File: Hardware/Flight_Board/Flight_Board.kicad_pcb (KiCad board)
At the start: 2 copper layers, 50.8 x 101.6 mm, 128 parts, among them J1 Conn_01x04, J2 Conn_01x08, J3 Conn_01x04, J4 Conn_01x06, J5 MEM2067-02-180-00-A_REVB, SW1 SW_Push, U1 FT5HN, U2 STM32F411RCTx, U3 ADXL375, U4 BMP390, U5 CAM-M8Q-0, U6 BMI323, U7 AP62200WU, U8 TPS274160A, U9 LR62E

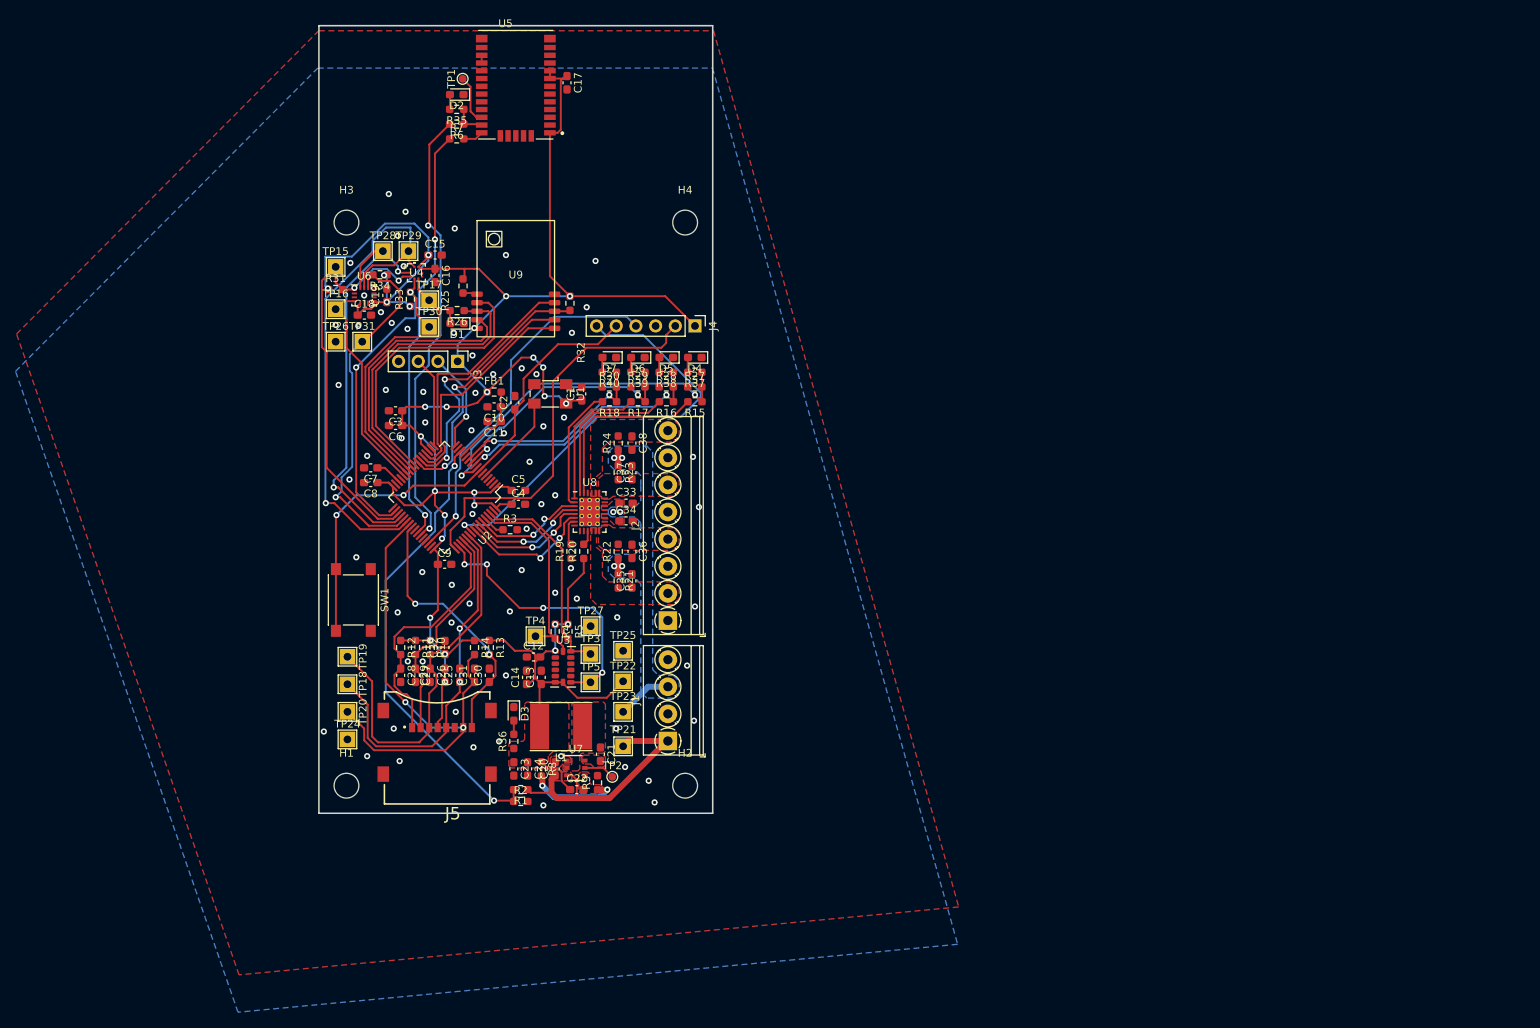
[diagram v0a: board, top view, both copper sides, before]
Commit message: begin 4 layer board
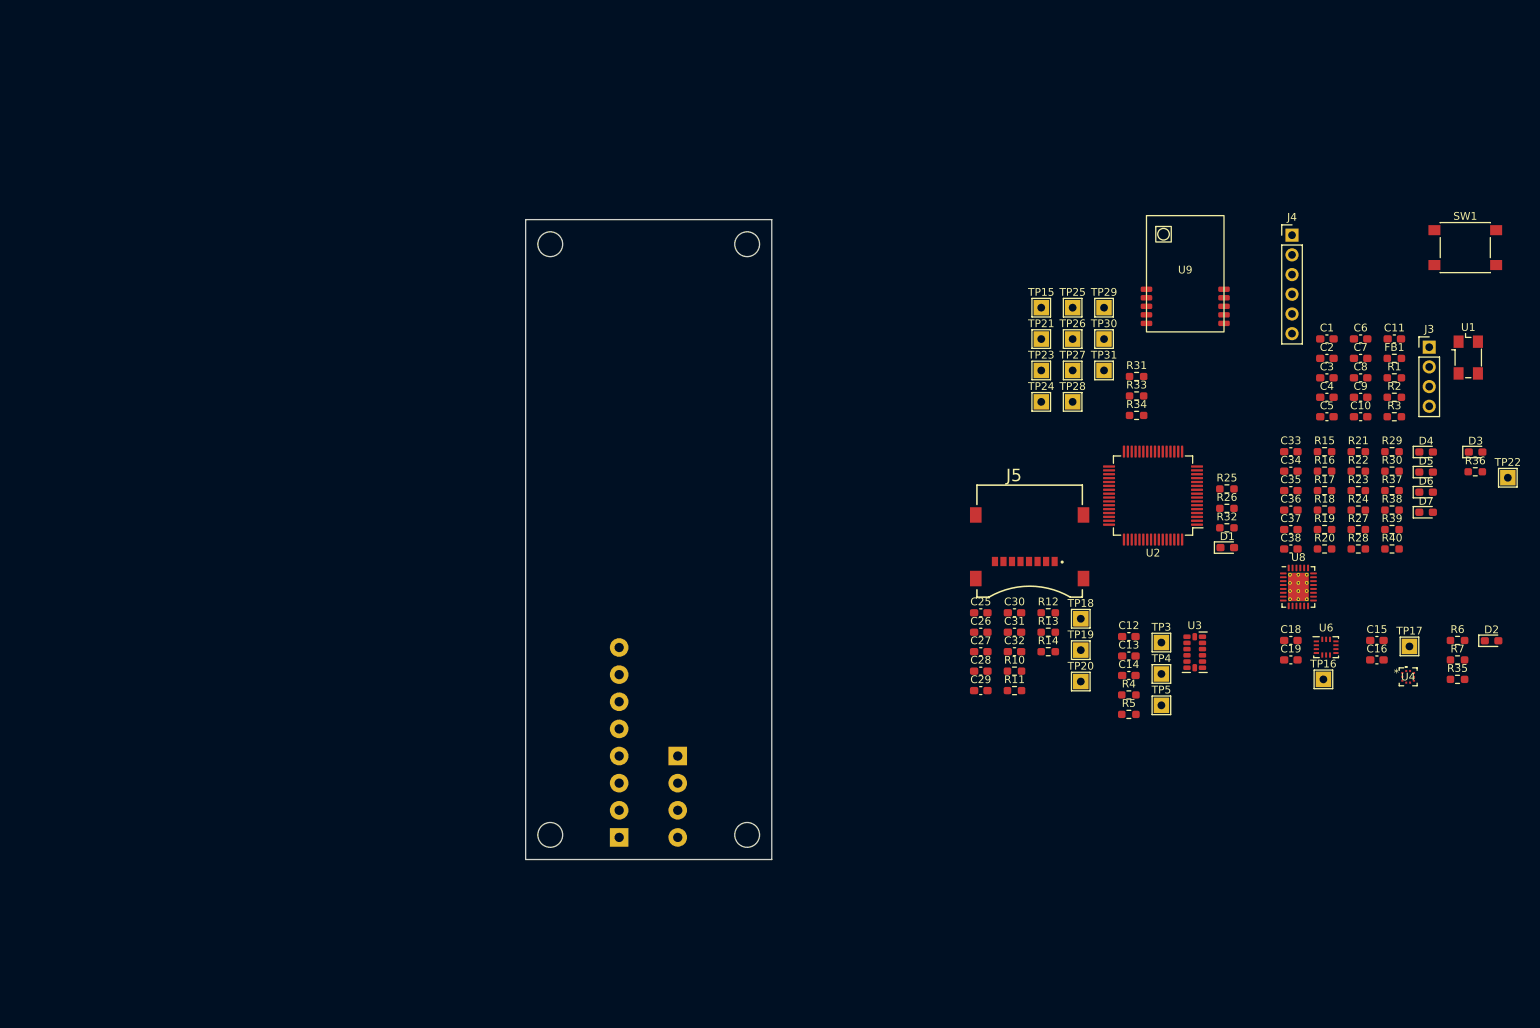
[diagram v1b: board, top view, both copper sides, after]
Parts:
- removed C17: 4.7u, Capacitor_SMD:C_0603_1608Metric_Pad1.08x0.95mm_HandSolder
- removed C20: 10u, Capacitor_SMD:C_0603_1608Metric_Pad1.08x0.95mm_HandSolder
- removed C21: 330n, Capacitor_SMD:C_0603_1608Metric_Pad1.08x0.95mm_HandSolder
- removed C22: 47p, Capacitor_SMD:C_0603_1608Metric_Pad1.08x0.95mm_HandSolder
- removed C23, C24: 22u, Capacitor_SMD:C_0603_1608Metric_Pad1.08x0.95mm_HandSolder
- removed L1: 4.7u, Inductor_SMD:L_Taiyo-Yuden_NR-60xx_HandSoldering
- removed R8: 31.6k, Resistor_SMD:R_0603_1608Metric_Pad0.98x0.95mm_HandSolder
- removed R9: 10k, Resistor_SMD:R_0603_1608Metric_Pad0.98x0.95mm_HandSolder
- removed TP1: SAFEBOOT, TestPoint:TestPoint_Pad_D1.0mm
- removed TP2: EN, TestPoint:TestPoint_Pad_D1.0mm
- removed U5: CAM-M8Q-0, Project:LCC100P960X1400X210-31N
- removed U7: AP62200WU, Package_SO:TSOP-6_1.65x3.05mm_P0.95mm
- H1, H2, H3, H4: footprint MountingHole:MountingHole_3.2mm_M3 -> MountingHole:MountingHole_3.2mm_M3_ISO14580
- J1, J2: moved to B.Cu
- moved D2 151.0 mm to (261.1, 117.8), turned to 0 degrees
- moved SW1 150.5 mm to (257.7, 67.1), turned to 0 degrees
- moved R35 148.6 mm to (256.7, 122.8), turned to 0 degrees
- moved R7 145.6 mm to (256.7, 120.3)
- moved R6 145.3 mm to (256.7, 117.8), turned to 0 degrees
- moved U4 138.2 mm to (250.4, 122.5)
- moved TP16 136.1 mm to (239.4, 122.8)
- moved TP17 134.1 mm to (250.5, 118.6)
- moved U6 132.1 mm to (239.8, 118.7)
- moved C15 131.3 mm to (246.3, 117.8)
- moved C16 131.2 mm to (246.3, 120.3), turned to 0 degrees
- moved R36 128.8 mm to (259.0, 96.0), turned to 0 degrees
- moved D3 128.6 mm to (259.1, 93.5), turned to 0 degrees
- moved C7 128.5 mm to (244.2, 81.4), turned to 0 degrees
- moved C8 128.4 mm to (244.2, 83.9), turned to 0 degrees
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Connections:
- R7 pad 2: Net-(U5-RXD/SPI_MOSI) -> unconnected-(R7-Pad2)
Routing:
- net +3.3V: track 308.4 -> 0.00 mm, vias 28 -> 0
- net /Barometer/SCK: track 68.4 -> 0.00 mm, vias 1 -> 0
- net /Microcontroller/NRST: track 64.8 -> 0.00 mm, vias 2 -> 0
- net /MicroSD/SDIO_D0: track 64.4 -> 0.00 mm, vias 2 -> 0
- net /GPS/TXD: track 60.2 -> 0.00 mm, vias 2 -> 0
- net /Microcontroller/VBAT_ADC: track 59.0 -> 0.00 mm, vias 2 -> 0
- net /Microcontroller/SWO: track 56.3 -> 0.00 mm, vias 1 -> 0
- net /Barometer/MOSI: track 55.6 -> 0.00 mm, vias 2 -> 0
- net /GPS/RXD: track 54.2 -> 0.00 mm, vias 2 -> 0
- net /Barometer/MISO: track 53.1 -> 0.00 mm, vias 2 -> 0
- net /Microcontroller/SWCLK: track 51.7 -> 0.00 mm
- net /MicroSD/SDIO_CMD: track 50.2 -> 0.00 mm
- net /IMU/~{CS}: track 47.4 -> 0.00 mm, vias 1 -> 0
- net /Microcontroller/SWDIO: track 47.1 -> 0.00 mm, vias 1 -> 0
- net /MicroSD/SDIO_CLK: track 46.7 -> 0.00 mm, vias 2 -> 0
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- added copper zone on In2.Cu, net +3.3V
- added copper zone on In1.Cu, net GND
- removed copper zone on F.Cu, net +3.3V
- removed copper zone on F.Cu, net /PYRO1
- removed copper zone on F.Cu, net /PYRO2
- removed copper zone on F.Cu, net /PYRO3
- removed copper zone on F.Cu, net /PYRO4
- removed copper zone on F.Cu, net /VBAT
- removed copper zone on B.Cu, net /VPYRO
- removed copper zone on F.Cu, net /VPYRO
- removed copper zone on B.Cu, net GND
- removed copper zone on F.Cu, net GND
- removed copper zone on F.Cu, net Net-(U7-BST)
- removed copper zone on F.Cu, net Net-(U7-FB)
- removed copper zone on F.Cu, net Net-(U7-SW)
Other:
- board size 50.8 x 101.6 mm -> 31.8 x 82.6 mm
- copper layers 2 -> 4

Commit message: initial route of 4-layer board
ouch
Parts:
- removed C2: 100n, Capacitor_SMD:C_0603_1608Metric_Pad1.08x0.95mm_HandSolder
- removed C37, C38: 22n, Capacitor_SMD:C_0603_1608Metric_Pad1.08x0.95mm_HandSolder
- removed D4: P1, LED_SMD:LED_0603_1608Metric_Pad1.05x0.95mm_HandSolder
- removed D5: P2, LED_SMD:LED_0603_1608Metric_Pad1.05x0.95mm_HandSolder
- removed D6: P3, LED_SMD:LED_0603_1608Metric_Pad1.05x0.95mm_HandSolder
- removed D7: P4, LED_SMD:LED_0603_1608Metric_Pad1.05x0.95mm_HandSolder
- removed R31, R32, R33, R34, R35, R36, R37, R38, R39, R40: 22k, Resistor_SMD:R_0603_1608Metric_Pad0.98x0.95mm_HandSolder
- removed SW1: SW_Push, Button_Switch_SMD:SW_SPST_PTS645
- removed TP15: MISO, TestPoint:TestPoint_THTPad_2.0x2.0mm_Drill1.0mm
- removed TP16: IMU_INT, TestPoint:TestPoint_THTPad_2.0x2.0mm_Drill1.0mm
- removed TP17: BARO_INT, TestPoint:TestPoint_THTPad_2.0x2.0mm_Drill1.0mm
- removed TP18: SD_CLK, TestPoint:TestPoint_THTPad_2.0x2.0mm_Drill1.0mm
- removed TP19: SD_CMD, TestPoint:TestPoint_THTPad_2.0x2.0mm_Drill1.0mm
- removed TP20: SD_D0, TestPoint:TestPoint_THTPad_2.0x2.0mm_Drill1.0mm
- removed TP21: VBAT, TestPoint:TestPoint_THTPad_2.0x2.0mm_Drill1.0mm
- removed TP22: 3V3, TestPoint:TestPoint_THTPad_2.0x2.0mm_Drill1.0mm
- removed TP23: VPYRO, TestPoint:TestPoint_THTPad_2.0x2.0mm_Drill1.0mm
- removed TP24, TP25, TP26, TP27: GND, TestPoint:TestPoint_THTPad_2.0x2.0mm_Drill1.0mm
- removed TP28: MOSI, TestPoint:TestPoint_THTPad_2.0x2.0mm_Drill1.0mm
- removed TP29: SCK, TestPoint:TestPoint_THTPad_2.0x2.0mm_Drill1.0mm
- removed TP3: SDA, TestPoint:TestPoint_THTPad_2.0x2.0mm_Drill1.0mm
- removed TP30: CS1, TestPoint:TestPoint_THTPad_2.0x2.0mm_Drill1.0mm
- removed TP31: CS2, TestPoint:TestPoint_THTPad_2.0x2.0mm_Drill1.0mm
- removed TP4: SCL, TestPoint:TestPoint_THTPad_2.0x2.0mm_Drill1.0mm
- removed TP5: ACC_INT, TestPoint:TestPoint_THTPad_2.0x2.0mm_Drill1.0mm
- added C17: 1u, Capacitor_SMD:C_0603_1608Metric_Pad1.08x0.95mm_HandSolder, F.Cu at (141.1, 70.9)
- added C20: 100n, Capacitor_SMD:C_0603_1608Metric_Pad1.08x0.95mm_HandSolder, F.Cu at (158.8, 94.4)
- added C21: 1u, Capacitor_SMD:C_0603_1608Metric_Pad1.08x0.95mm_HandSolder, F.Cu at (159.9, 134.2)
- added C22: 2.2u, Capacitor_SMD:C_0603_1608Metric_Pad1.08x0.95mm_HandSolder, F.Cu at (159.9, 137.8)
- added C23: 22p, Capacitor_SMD:C_0603_1608Metric_Pad1.08x0.95mm_HandSolder, F.Cu at (158.9, 126.7)
- added C24: 22p, Capacitor_SMD:C_0603_1608Metric_Pad1.08x0.95mm_HandSolder, F.Cu at (162.6, 126.7)
- added FB2: FerriteBead, Resistor_SMD:R_0603_1608Metric_Pad0.98x0.95mm_HandSolder, F.Cu at (141.1, 74.3)
- added R8: 4.7k, Resistor_SMD:R_0603_1608Metric_Pad0.98x0.95mm_HandSolder, F.Cu at (164.5, 83.9)
- added R9: 220, Resistor_SMD:R_0603_1608Metric_Pad0.98x0.95mm_HandSolder, F.Cu at (141.1, 79.4)
- added U5: FGPMMOPA6H, Project:FGPMMOPA6H, F.Cu at (144.5, 64.3)
- added U7: AP2205-33Y-13, Package_TO_SOT_SMD:SOT-89-3, F.Cu at (163.8, 136.0)
- C27: value 22p -> 10u
- C29: value 10u -> 22p
- C30: value 22p -> 100n
- C31: value 22p -> 10n
- C33: value 10n -> 22n
- C34: value 100n -> 22n
- D1: value BUSY -> GPS_TX
- D2: value GPS_TX -> POWER
- D3: value POWER -> BUSY
- J5: moved to B.Cu
- R10: value 10k -> 220
- R11, R12, R2, R25, R27, R28, R3, R30: value 10k -> 22k
- R15, R16, R17, R5: value 4.7k -> 10k
- R19: value 1k -> 4.7k
- R20: value 10k -> 4.7k
- R21: value 22k -> 4.7k
- R22: value 22k -> 1k
- R23: value 22k -> 10k
- R4: value 4.7k -> 22k
- R6: value 220 -> 10k
- R7: value 220 -> 4.7k
- U8: footprint Package_DFN_QFN:QFN-28-1EP_4x5mm_P0.5mm_EP2.65x3.65mm_ThermalVias -> Project:TPS274160A
- moved U1 117.4 mm to (141.6, 95.9), turned to 90 degrees
- moved J3 116.0 mm to (138.8, 100.1)
- moved D2 111.6 mm to (152.4, 142.7)
- moved R22 111.2 mm to (141.0, 138.0), turned to 90 degrees
- moved FB1 109.1 mm to (141.7, 103.4), turned to 90 degrees
- moved R23 109.1 mm to (141.0, 134.5), turned to 90 degrees
- moved C11 108.9 mm to (141.7, 99.9), turned to 90 degrees
- moved R21 108.7 mm to (138.6, 120.3), turned to -90 degrees
- moved R24 106.4 mm to (144.4, 138.4), turned to -90 degrees
- moved D3 105.0 mm to (154.2, 88.0), turned to -90 degrees
- moved R7 104.9 mm to (158.9, 82.7), turned to 90 degrees
- moved C7 104.7 mm to (144.8, 114.2), turned to -90 degrees
- moved C18 104.4 mm to (141.1, 72.6)
- moved C1 103.6 mm to (137.7, 95.9), turned to -90 degrees
- moved C6 103.4 mm to (147.3, 115.1), turned to 180 degrees
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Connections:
- C18 pad 1: +3.3V -> Net-(U5-VCC)
- C25 pad 1: /MicroSD/SDIO_CLK -> /MicroSD/SDIO_D3
- C26 pad 1: /MicroSD/SDIO_CMD -> /MicroSD/SDIO_D2
- C27 pad 1: /MicroSD/SDIO_D3 -> +3.3V
- C28 pad 1: /MicroSD/SDIO_D2 -> /MicroSD/SDIO_D1
- C29 pad 1: +3.3V -> /MicroSD/SDIO_D0
- C30 pad 1: /MicroSD/SDIO_D1 -> +3.3V
- C31 pad 1: /MicroSD/SDIO_D0 -> /VPYRO
- C32 pad 1: +3.3V -> /VPYRO
- C33 pad 1: /VPYRO -> /PYRO4
- C34 pad 1: /VPYRO -> /PYRO3
- C35 pad 1: /PYRO4 -> /PYRO2
- C36 pad 1: /PYRO3 -> /PYRO1
- R1 pad 1: /VBAT -> +3.3V
- R1 pad 2: /Microcontroller/VBAT_ADC -> /Barometer/MISO
- R10 pad 1: +3.3V -> /GPS/RXD
- R10 pad 2: /MicroSD/SDIO_CMD -> Net-(U5-RX)
- R11 pad 1: +3.3V -> Net-(U5-TX)
- R11 pad 2: /MicroSD/SDIO_D3 -> Net-(D1-A)
- R12 pad 2: /MicroSD/SDIO_D2 -> Net-(D2-A)
- R13 pad 2: /MicroSD/SDIO_D1 -> /MicroSD/SDIO_CMD
- R14 pad 2: /MicroSD/SDIO_D0 -> /MicroSD/SDIO_D3
- R15 pad 1: /Current Switch/EN1 -> +3.3V
- R15 pad 2: Net-(U8-EN1) -> /MicroSD/SDIO_D2
- R16 pad 1: /Current Switch/EN2 -> +3.3V
- R16 pad 2: Net-(U8-EN2) -> /MicroSD/SDIO_D1
- R17 pad 1: /Current Switch/EN3 -> +3.3V
- R17 pad 2: Net-(U8-EN3) -> /MicroSD/SDIO_D0
- R18 pad 1: /Current Switch/EN4 -> /Current Switch/EN1
- R18 pad 2: Net-(U8-EN4) -> Net-(U8-EN1)
- R19 pad 1: GND -> /Current Switch/EN2
- R19 pad 2: Net-(U8-CL) -> Net-(U8-EN2)
- R2 pad 1: /Microcontroller/VBAT_ADC -> +3.3V
- R2 pad 2: GND -> /CS1
- R20 pad 1: +3.3V -> /Current Switch/EN3
- R20 pad 2: Net-(U8-DIAG_EN) -> Net-(U8-EN3)
- R21 pad 1: /VPYRO -> /Current Switch/EN4
- R21 pad 2: /PYRO4 -> Net-(U8-EN4)
- R22 pad 1: /VPYRO -> GND
- R22 pad 2: /PYRO3 -> Net-(U8-CL)
- R23 pad 1: /VPYRO -> +3.3V
- R23 pad 2: /PYRO2 -> Net-(U8-DIAG_EN)
- R24 pad 2: /PYRO1 -> /PYRO4
- R25 pad 1: +3.3V -> /VPYRO
- R25 pad 2: Net-(U9-ANT_SW) -> /PYRO3
- R26 pad 1: /LoRa/LORA_BUSY -> /VPYRO
- R26 pad 2: Net-(D1-A) -> /PYRO2
- R27 pad 1: GND -> /VPYRO
- R27 pad 2: /Current Switch/EN1 -> /PYRO1
- R28 pad 1: GND -> /LoRa/LORA_BUSY
- R28 pad 2: /Current Switch/EN2 -> Net-(D3-A)
- R29 pad 1: GND -> +3.3V
- R29 pad 2: /Current Switch/EN3 -> Net-(U9-ANT_SW)
- R3 pad 1: Net-(U2-BOOT0) -> +3.3V
- R3 pad 2: GND -> /CS2
- R30 pad 1: GND -> +3.3V
- R30 pad 2: /Current Switch/EN4 -> /LoRa/LORA_MISO
- R4 pad 1: +3.3V -> /VBAT
- R4 pad 2: /Accelerometer/SCL -> /Microcontroller/VBAT_ADC
- R5 pad 1: +3.3V -> /Microcontroller/VBAT_ADC
- R5 pad 2: /Accelerometer/SDA -> GND
- R6 pad 1: Net-(R35-Pad1) -> Net-(U2-BOOT0)
- R6 pad 2: /GPS/TXD -> GND
- R7 pad 1: /GPS/RXD -> +3.3V
- R7 pad 2: unconnected-(R7-Pad2) -> /Accelerometer/SCL
- U2 pad 34: /Barometer/~{CS} -> /CS1
- U2 pad 37: /IMU/~{CS} -> /CS2
- U4 pad 6: /Barometer/~{CS} -> /CS1
- U6 pad 12: /IMU/~{CS} -> /CS2
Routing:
- net GND: track 0.00 -> 155.4 mm, vias 0 -> 46
- net +3.3V: track 0.00 -> 93.6 mm, vias 0 -> 26
- net /CS2: track 0.00 -> 51.5 mm, vias 0 -> 4
- net /Current Switch/~{ST1}: track 0.00 -> 44.0 mm, vias 0 -> 2
- net /Current Switch/~{ST2}: track 0.00 -> 43.2 mm, vias 0 -> 2
- net /GPS/RXD: track 0.00 -> 40.6 mm, vias 0 -> 2
- net /Current Switch/~{ST4}: track 0.00 -> 40.1 mm, vias 0 -> 2
- net /Barometer/INT: track 0.00 -> 40.0 mm, vias 0 -> 3
- net /Current Switch/~{ST3}: track 0.00 -> 39.9 mm, vias 0 -> 2
- net /Microcontroller/VBAT_ADC: track 0.00 -> 39.7 mm, vias 0 -> 2
- net /GPS/TXD: track 0.00 -> 39.5 mm, vias 0 -> 2
- net /Barometer/MISO: track 0.00 -> 36.1 mm, vias 0 -> 3
- net /Barometer/SCK: track 0.00 -> 35.8 mm, vias 0 -> 2
- net /Barometer/MOSI: track 0.00 -> 35.2 mm, vias 0 -> 3
- net /LoRa/LORA_MISO: track 0.00 -> 34.8 mm, vias 0 -> 2
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- added copper zone on F.Cu, net /PYRO1
- added copper zone on F.Cu, net /PYRO2
- added copper zone on F.Cu, net /PYRO3
- added copper zone on F.Cu, net /PYRO4
- added copper zone on F.Cu, net /VPYRO
- added copper zone on In2.Cu, net /VPYRO
- added copper zone on B.Cu, net GND
- added copper zone on F.Cu, net GND

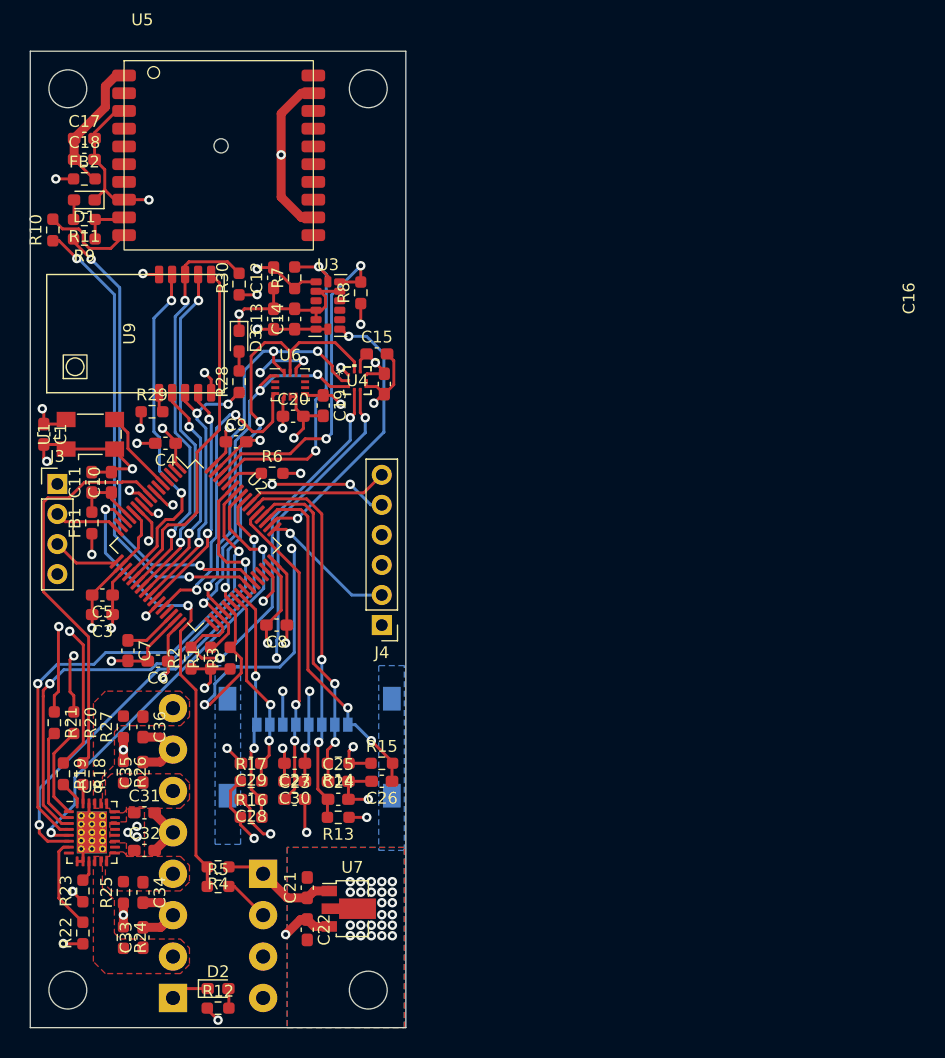
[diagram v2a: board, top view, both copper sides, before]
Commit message: silkscreen cleanup
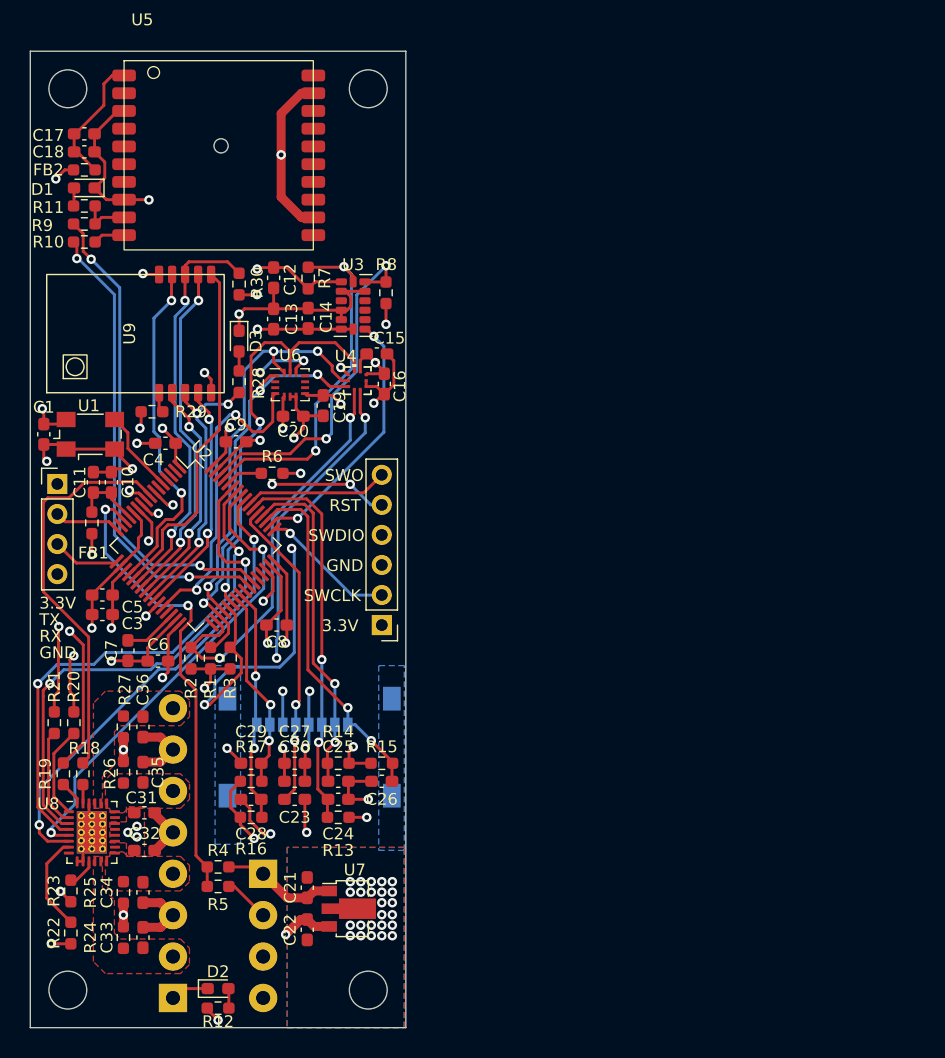
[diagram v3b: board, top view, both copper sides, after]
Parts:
- C12, C13: value 0.1u -> 100n
- moved R10 2.85 mm to (141.1, 79.6), turned to 0 degrees
- moved R8 2.13 mm to (166.6, 83.9)
- moved U3 2.13 mm to (163.8, 85.0)
- moved R9 1.27 mm to (141.1, 78.1)
- moved C14 1.14 mm to (160.0, 86.1)
- moved R7 1.14 mm to (160.0, 82.7)
- moved R11 1.14 mm to (141.1, 76.6)
- moved D1 1.02 mm to (141.1, 75.1)
- moved R22 1.02 mm to (140.0, 138.0)
- moved R23 1.02 mm to (140.0, 134.5)
- moved FB2 0.76 mm to (141.1, 73.5)
- moved C18 0.64 mm to (141.1, 72.0)
- moved C17 0.38 mm to (141.1, 70.5)
- moved C11 0.13 mm to (141.9, 99.9)
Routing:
- net Net-(U5-RX): track 7.95 -> 2.68 mm
- net +3.3V: track 93.6 -> 98.2 mm
- net GND: track 155.4 -> 157.4 mm
- net /Accelerometer/SCL: track 28.6 -> 30.6 mm
- net /Accelerometer/INT1: track 24.1 -> 22.4 mm
- net /GPS/TXD: track 39.5 -> 40.8 mm
- net /GPS/RXD: track 40.6 -> 39.5 mm
- net /Accelerometer/SDA: track 29.2 -> 30.1 mm
- net Net-(U8-DIAG_EN): track 1.80 -> 2.50 mm
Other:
- board text added: "-"
- board text added: "1+"
- board text added: "2+"
- board text added: "3+"
- board text added: "3.3V"
- board text added: "4+"
- board text added: "B+"
- board text added: "GND"
- board text added: "P+"
- board text added: "RST"
- board text added: "RX"
- board text added: "Rocket Flight Computer v1 William Hutchinson RyLynd Bullington Ryan Parker Ethan Baranczuk"
- board text added: "SWCLK"
- board text added: "SWDIO"
- board text added: "SWO"
- board text added: "TX"
